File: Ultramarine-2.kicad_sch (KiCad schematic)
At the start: 108 parts, among them J1 OLED, J2 Flex LED 3V, J3 Generic_connector, J4 Flex LED GND, SW1 SW_Push, SW10 SW_Push, SW11 SW_Push, SW12 SW_Push, SW13 SW_Push, SW14 SW_Push, SW15 SW_Push, SW16 SW_Push, SW17 SW_Push, SW18 SW_Push, SW19 SW_Push, SW2 SW_Push, SW20 SW_Push, SW21 SW_Push, SW22 SW_Push, SW23 SW_Push, SW24 SW_Push, SW25 SW_Push, SW26 SW_Push, SW27 SW_Push, SW28 SW_Push, SW29 SW_Push, SW3 SW_Push, SW30 SW_Push, SW31 RotaryEncoder_Switch, SW32 Reset, SW4 SW_Push, SW5 SW_Push, SW6 SW_Push, SW7 SW_Push, SW8 SW_Push, SW9 SW_Push

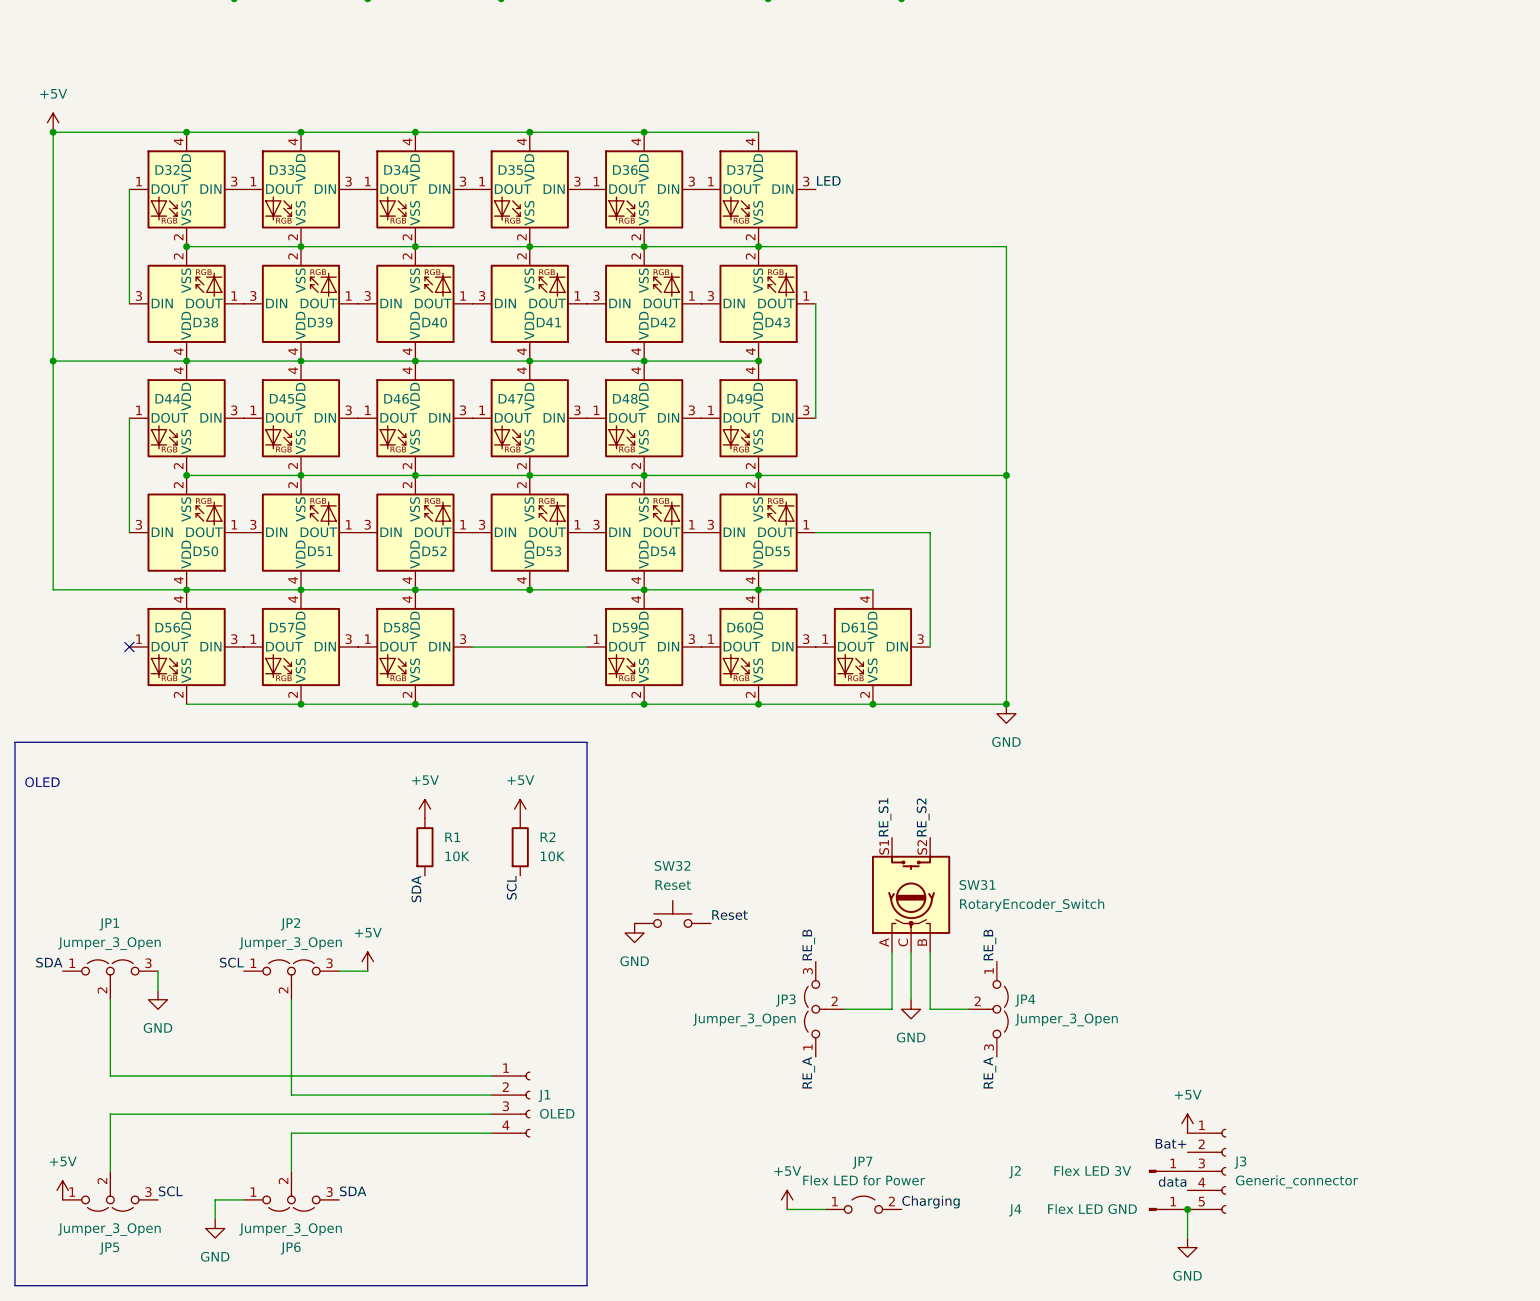
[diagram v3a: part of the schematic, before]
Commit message: Changed to 6pin connector
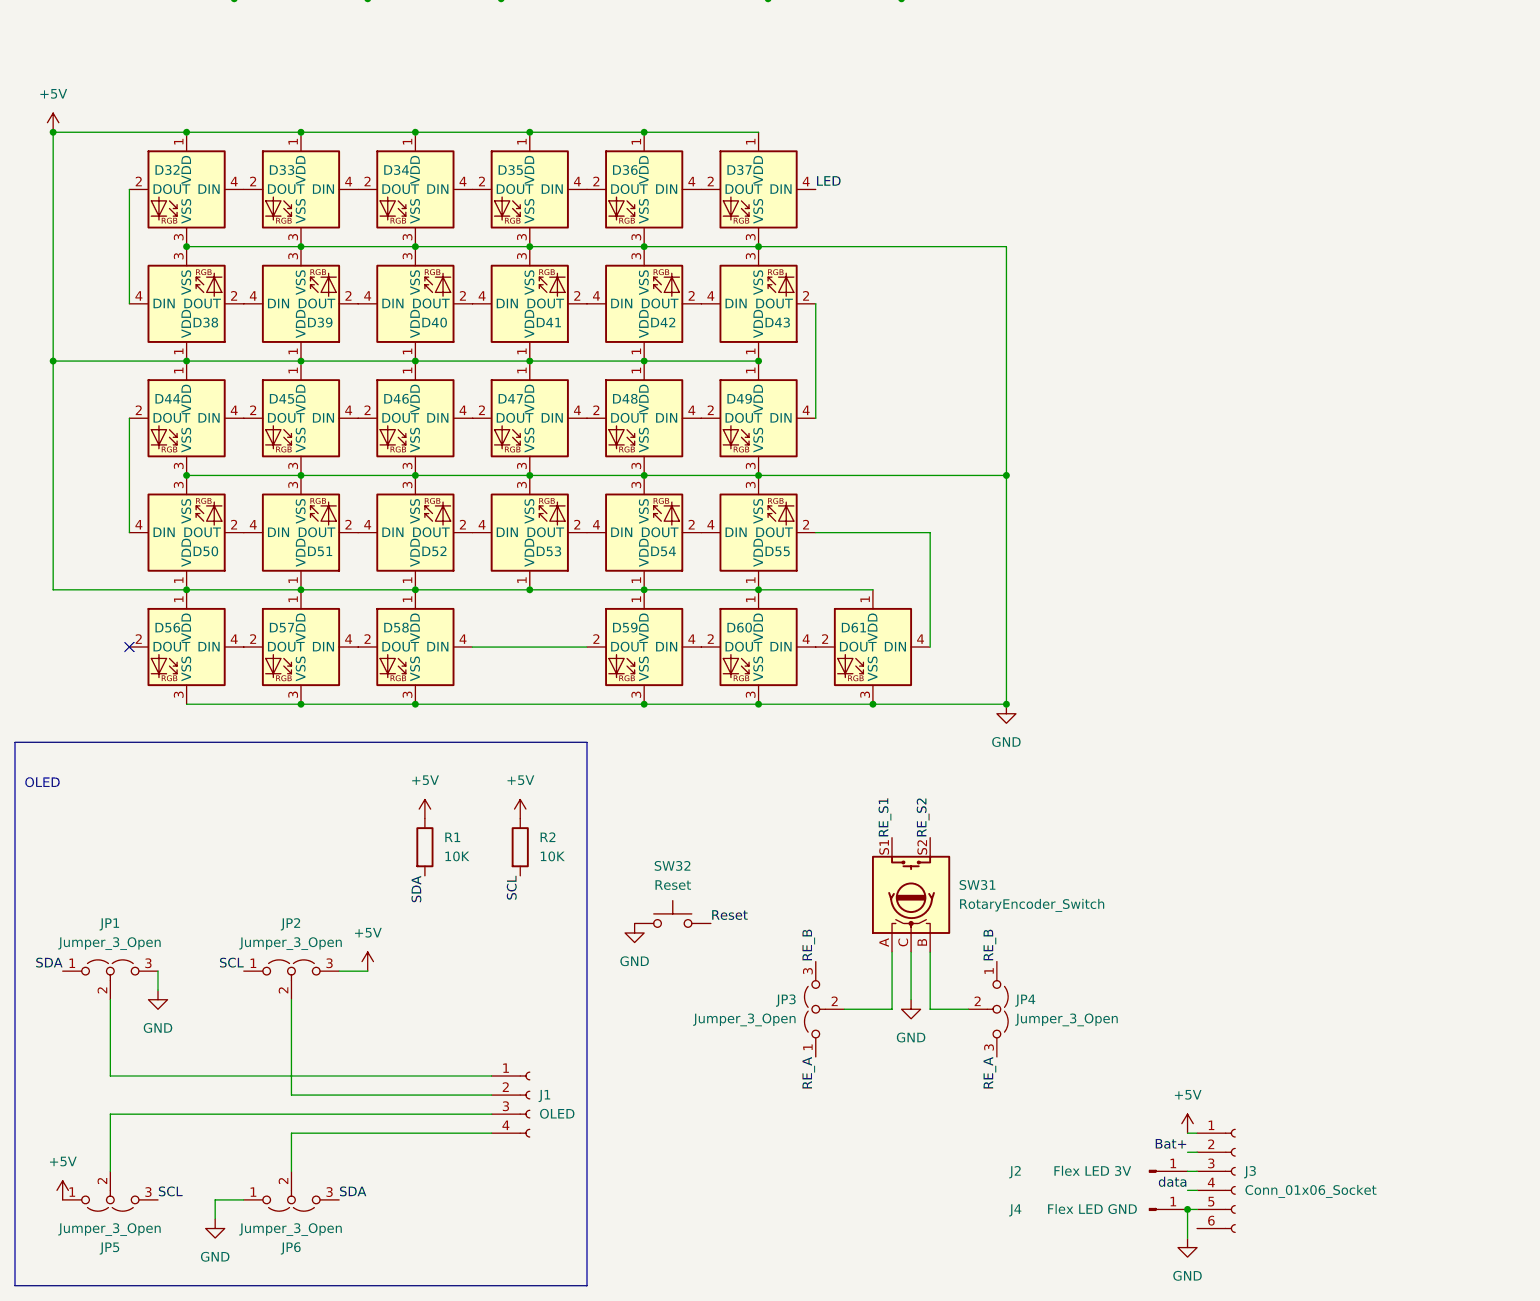
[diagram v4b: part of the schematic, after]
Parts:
- removed J3: Generic_connector, Ultramarine-2:5pin, symbol Connector:Conn_01x05_Socket
- removed JP7: Flex LED for Power, Jumper:SolderJumper-2_P1.3mm_Open_TrianglePad1.0x1.5mm, symbol Jumper:Jumper_2_Open
- added J3: Conn_01x06_Socket, Ultramarine-2:JST_ZH_6, symbol Connector:Conn_01x06_Socket
- D32, D33, D34, D35, D36, D37, D38, D39, D40, D41, D42, D43, D44, D45, D46, D47, D48, D49, D50, D51, D52, D53, D54, D55, D56, D57, D58, D59, D60, D61: value SK6812MINI -> SK6812-mini-e; footprint Ultramarine-2:SK6812-mini -> Ultramarine-2:SK6812-mini-e; symbol LED:SK6812MINI -> Ultramarine-2:SK6812-mini-e
- SW32: footprint Ultramarine-2:Tactlie_Switch -> Ultramarine-2:TVAF06
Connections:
- net +5V: now also D32.1 (VDD), D33.1 (VDD), D34.1 (VDD), D35.1 (VDD), D36.1 (VDD), D37.1 (VDD), D38.1 (VDD), D39.1 (VDD), D40.1 (VDD), D41.1 (VDD), D42.1 (VDD), D43.1 (VDD), D44.1 (VDD), D45.1 (VDD), D46.1 (VDD), D47.1 (VDD), D48.1 (VDD), D49.1 (VDD), D50.1 (VDD), D51.1 (VDD), D52.1 (VDD), D53.1 (VDD), D54.1 (VDD), D55.1 (VDD), D56.1 (VDD), D57.1 (VDD), D58.1 (VDD), D59.1 (VDD), D60.1 (VDD), D61.1 (VDD), J3.1 (Pin_1); no longer D32.4 (VDD), D33.4 (VDD), D34.4 (VDD), D35.4 (VDD), D36.4 (VDD), D37.4 (VDD), D38.4 (VDD), D39.4 (VDD), D40.4 (VDD), D41.4 (VDD), D42.4 (VDD), D43.4 (VDD), D44.4 (VDD), D45.4 (VDD), D46.4 (VDD), D47.4 (VDD), D48.4 (VDD), D49.4 (VDD), D50.4 (VDD), D51.4 (VDD), D52.4 (VDD), D53.4 (VDD), D54.4 (VDD), D55.4 (VDD), D56.4 (VDD), D57.4 (VDD), D58.4 (VDD), D59.4 (VDD), D60.4 (VDD), D61.4 (VDD)
- net Bat+: now also J3.2 (Pin_2)
- net GND: now also D32.3 (VSS), D33.3 (VSS), D34.3 (VSS), D35.3 (VSS), D36.3 (VSS), D37.3 (VSS), D38.3 (VSS), D39.3 (VSS), D40.3 (VSS), D41.3 (VSS), D42.3 (VSS), D43.3 (VSS), D44.3 (VSS), D45.3 (VSS), D46.3 (VSS), D47.3 (VSS), D48.3 (VSS), D49.3 (VSS), D50.3 (VSS), D51.3 (VSS), D52.3 (VSS), D53.3 (VSS), D54.3 (VSS), D55.3 (VSS), D56.3 (VSS), D57.3 (VSS), D58.3 (VSS), D59.3 (VSS), D60.3 (VSS), D61.3 (VSS), J3.5 (Pin_5); no longer D32.2 (VSS), D33.2 (VSS), D34.2 (VSS), D35.2 (VSS), D36.2 (VSS), D37.2 (VSS), D38.2 (VSS), D39.2 (VSS), D40.2 (VSS), D41.2 (VSS), D42.2 (VSS), D43.2 (VSS), D44.2 (VSS), D45.2 (VSS), D46.2 (VSS), D47.2 (VSS), D48.2 (VSS), D49.2 (VSS), D50.2 (VSS), D51.2 (VSS), D52.2 (VSS), D53.2 (VSS), D54.2 (VSS), D55.2 (VSS), D56.2 (VSS), D57.2 (VSS), D58.2 (VSS), D59.2 (VSS), D60.2 (VSS), D61.2 (VSS)
- net LED: now also D37.4 (DIN); no longer D37.3 (DIN)
- net data: now also J3.4 (Pin_4)
- net at J2.1 (Pin_1): now also J3.3 (Pin_3)
- new net: D59.4 (DIN), D60.2 (DOUT)
- new net: D60.4 (DIN), D61.2 (DOUT)
- new net: D35.4 (DIN), D36.2 (DOUT)
- new net: D36.4 (DIN), D37.2 (DOUT)
- new net: D40.2 (DOUT), D41.4 (DIN)
- new net: D39.2 (DOUT), D40.4 (DIN)
- new net: D34.4 (DIN), D35.2 (DOUT)
- new net: D56.4 (DIN), D57.2 (DOUT)
- new net: D57.4 (DIN), D58.2 (DOUT)
- new net: D54.2 (DOUT), D55.4 (DIN)
- new net: D53.2 (DOUT), D54.4 (DIN)
- new net: D38.2 (DOUT), D39.4 (DIN)
- new net: D32.2 (DOUT), D38.4 (DIN)
- new net: D32.4 (DIN), D33.2 (DOUT)
- new net: D33.4 (DIN), D34.2 (DOUT)
- new net: D44.4 (DIN), D45.2 (DOUT)
- new net: D45.4 (DIN), D46.2 (DOUT)
- new net: D52.2 (DOUT), D53.4 (DIN)
- new net: D51.2 (DOUT), D52.4 (DIN)
- new net: D47.4 (DIN), D48.2 (DOUT)
- new net: D48.4 (DIN), D49.2 (DOUT)
- new net: D58.4 (DIN), D59.2 (DOUT)
- new net: D50.2 (DOUT), D51.4 (DIN)
- new net: D46.4 (DIN), D47.2 (DOUT)
- new net: D42.2 (DOUT), D43.4 (DIN)
- new net: D41.2 (DOUT), D42.4 (DIN)
- new net: D55.2 (DOUT), D61.4 (DIN)
- new net: D43.2 (DOUT), D49.4 (DIN)
- new net: D44.2 (DOUT), D50.4 (DIN)
